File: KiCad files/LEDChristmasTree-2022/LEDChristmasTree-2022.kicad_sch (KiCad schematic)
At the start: 26 parts, among them SW1 SW_SPDT

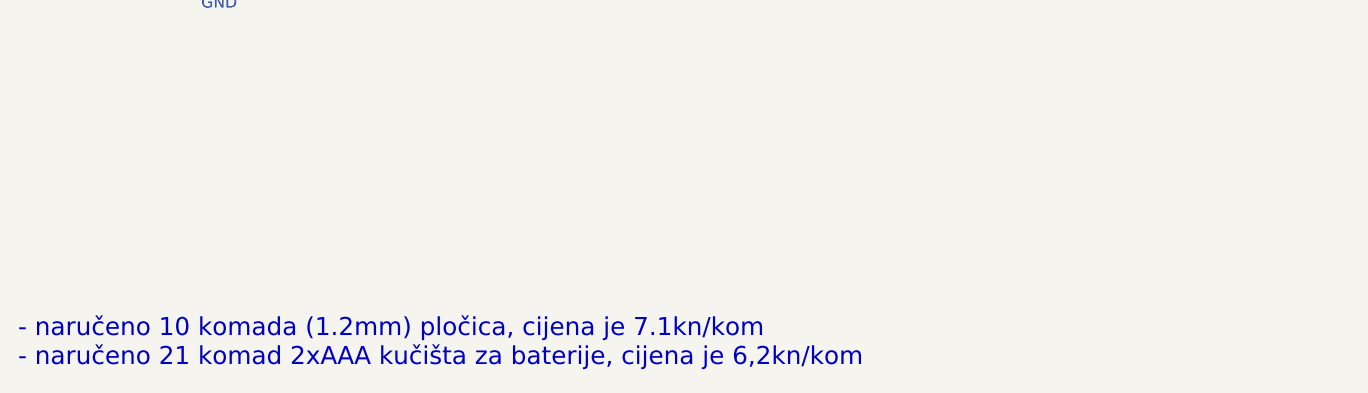
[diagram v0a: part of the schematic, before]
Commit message: Update LEDChristmasTree-2022.kicad_sch
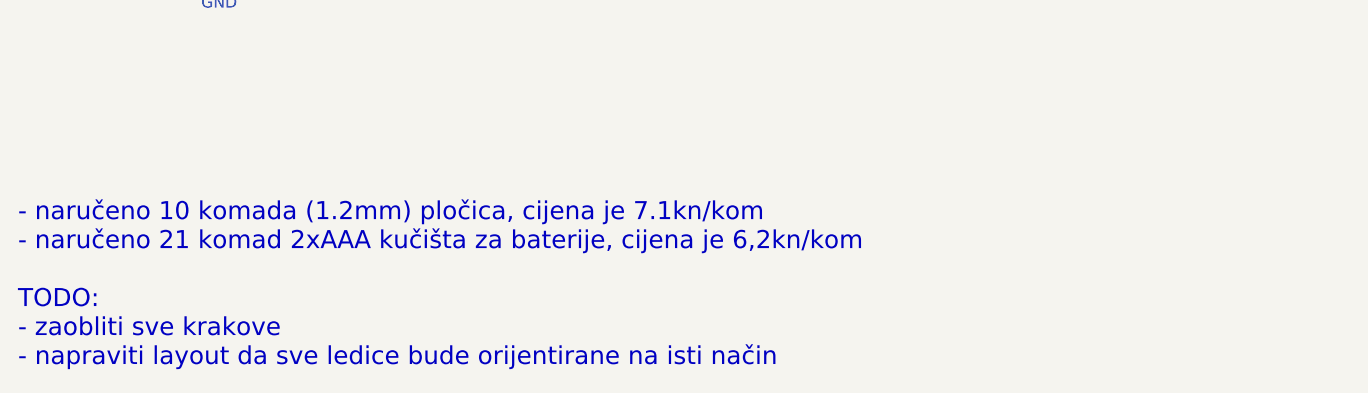
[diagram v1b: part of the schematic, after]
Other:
- note added: "- naručeno 10 komada (1.2mm) pločica, cijena je 7.1kn/kom - naručeno 21 komad 2xAAA kučišta za baterije, cijena je 6,2kn/kom TODO: - zaobliti sve krakove - napraviti layout da sve ledice bude orijentirane na isti način"
- note removed: "- naručeno 10 komada (1.2mm) pločica, cijena je 7.1kn/kom - naručeno 21 komad 2xAAA kučišta za baterije, cijena je 6,2kn/kom"
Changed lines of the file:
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@@
     (stroke (width 0) (type default) (color 0 0 0 0))
   )
-  (text "- naručeno 10 komada (1.2mm) pločica, cijena je 7.1kn/kom\n- naručeno 21 komad 2xAAA kučišta za baterije, cijena je 6,2kn/kom"
+  (text "- naručeno 10 komada (1.2mm) pločica, cijena je 7.1kn/kom\n- naručeno 21 komad 2xAAA kučišta za baterije, cijena je 6,2kn/kom\n\nTODO:\n- zaobliti sve krakove\n- napraviti layout da sve ledice bude orijentirane na isti način"
     (at 56.515 135.89 0)
     (effects (font (size 2 2)) (justify left bottom))
